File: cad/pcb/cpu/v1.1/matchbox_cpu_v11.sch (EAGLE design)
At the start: 61 parts, among them CN1 SM02B-SRSS-TB, P1 DF12-32-DP, P2 DF12-32-DP, Q1 FDN360P, Q2 FDN360P, U1 STM32F415R, U2 MCP1703, U3 MCP73831, U4 LTC2954-2, Y1 16MHz(9pF)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

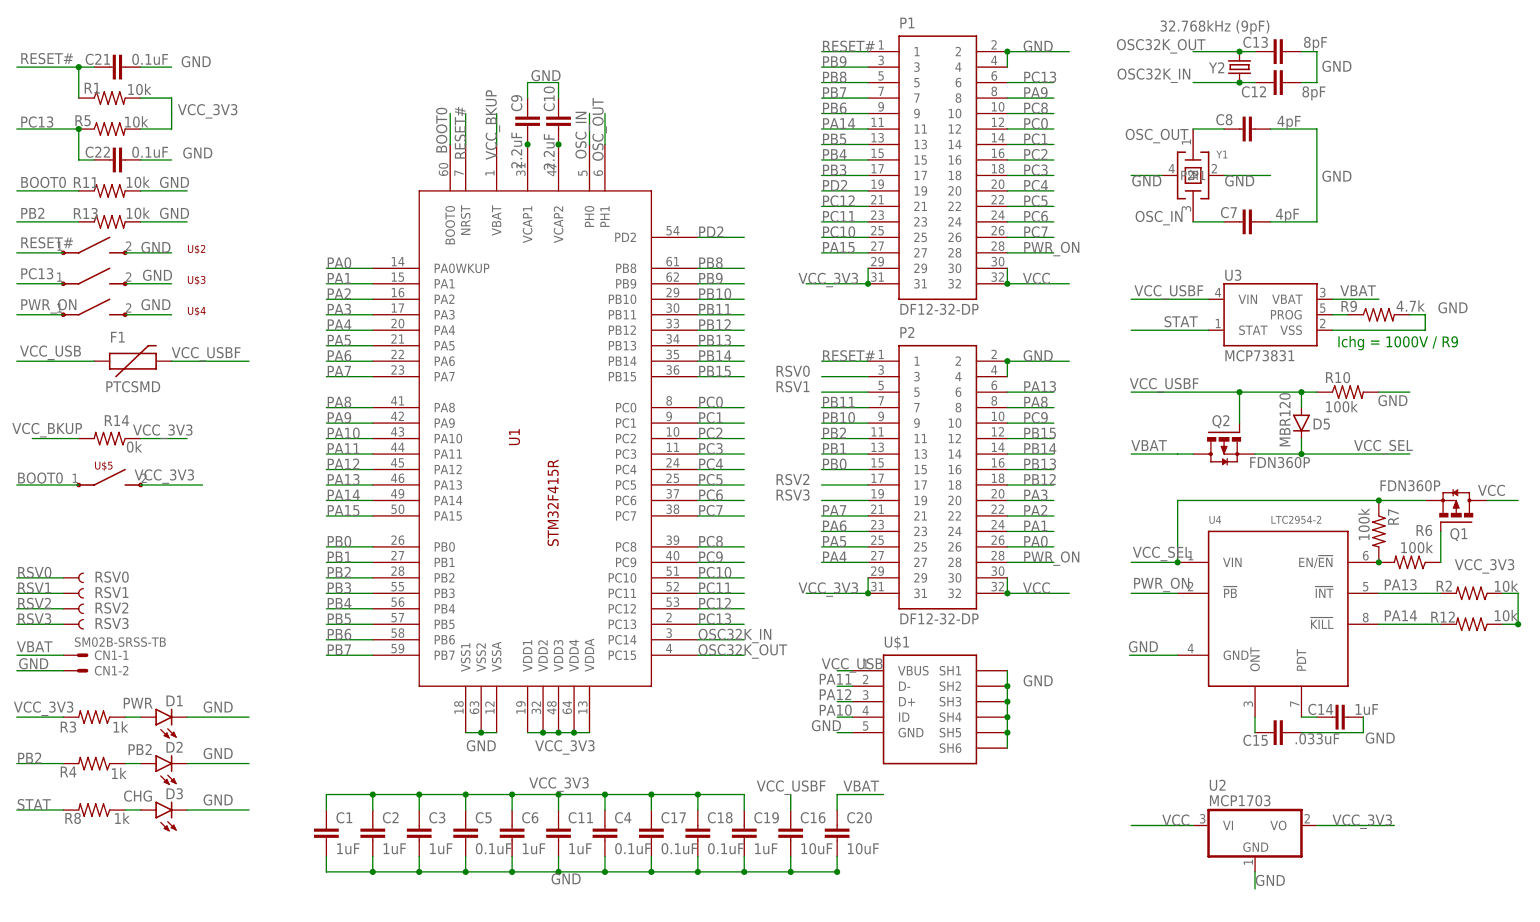
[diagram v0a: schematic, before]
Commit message: Side button improvement
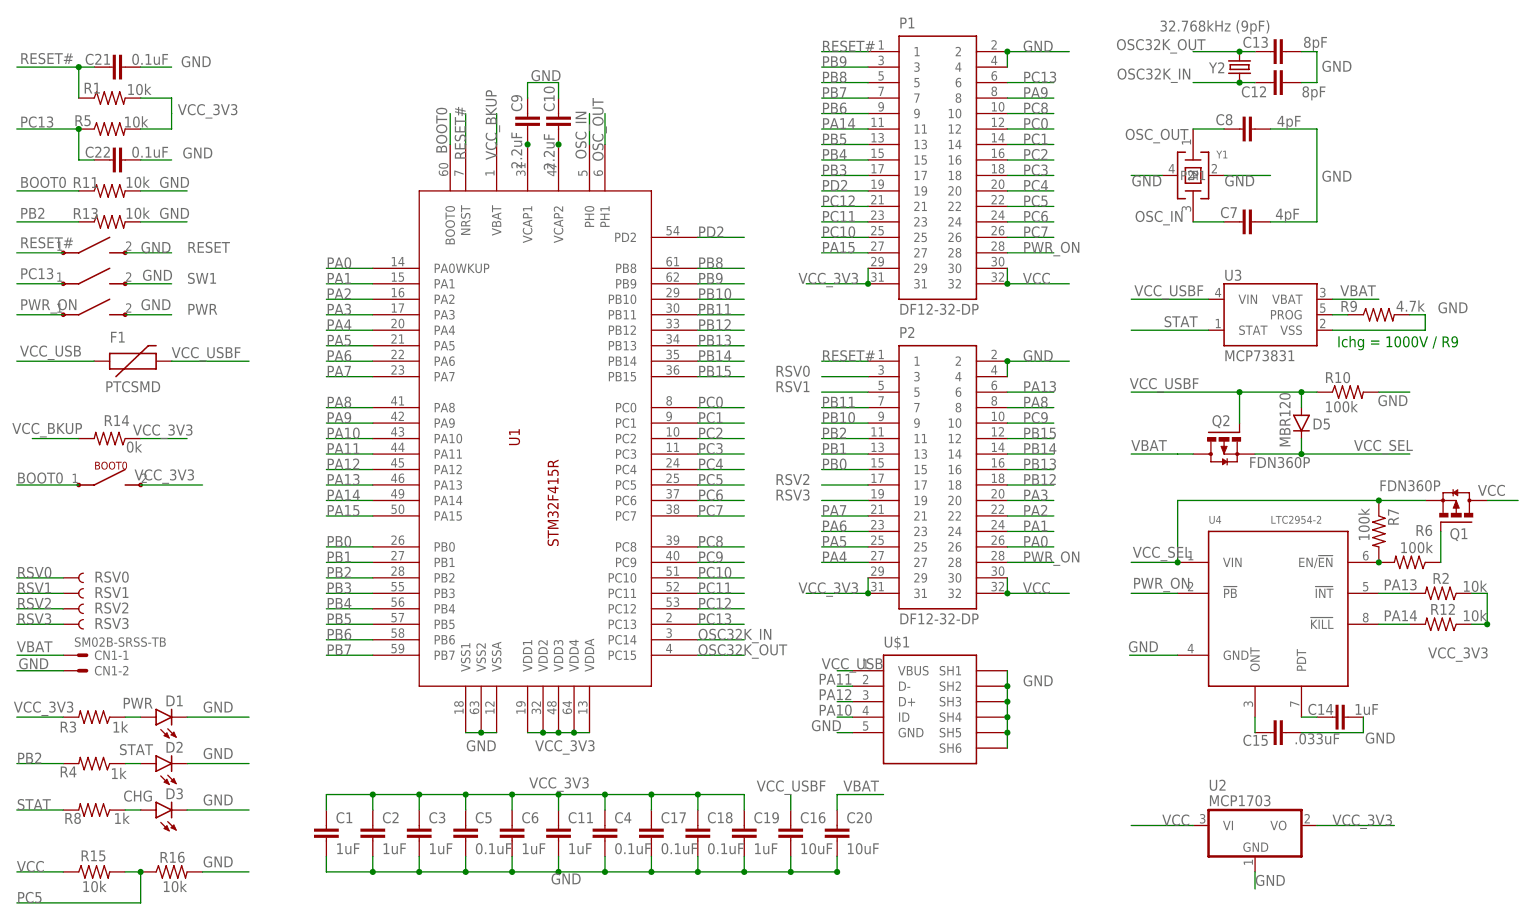
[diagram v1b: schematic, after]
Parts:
- added R15, R16: 10k, SparkFun-Passives:RESISTOR0805-RES
- D2: value PB2 -> STAT
- renumbered U$2 to RESET, U$3 to SW1, U$4 to PWR, U$5 to BOOT0
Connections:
- net GND: now also R16.2
- net PC5: now also R15.2, R16.1
- net VCC: now also R15.1
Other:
- moved on the sheet: R12, R2
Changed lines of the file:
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@@
 <part name="C15" library="SparkFun-Capacitors" deviceset="CAP" device="0805" value=".033uF"/>
 <part name="D1" library="SparkFun-LED" deviceset="LED" device="0603" value="PWR"/>
-<part name="D2" library="SparkFun-LED" deviceset="LED" device="0603" value="PB2"/>
+<part name="D2" library="SparkFun-LED" deviceset="LED" device="0603" value="STAT"/>
 <part name="R3" library="SparkFun-Passives" deviceset="RESISTOR" device="0805-RES" value="1k"/>
 <part name="R4" library="SparkFun-Passives" deviceset="RESISTOR" device="0805-RES" value="1k"/>
@@
 <part name="C22" library="SparkFun-Capacitors" deviceset="CAP" device="0805" value="0.1uF"/>
 <part name="U$1" library="jimduino" deviceset="MICROUSB" device=""/>
-<part name="U$2" library="sharp_display" deviceset="B3U-3100PM-B" device=""/>
-<part name="U$3" library="sharp_display" deviceset="B3U-3100PM-B" device=""/>
-<part name="U$4" library="sharp_display" deviceset="B3U-3100PM-B" device=""/>
-<part name="U$5" library="sharp_display" deviceset="B3U-3100PM-B" device=""/>
+<part name="RESET" library="sharp_display" deviceset="B3U-3100PM-B" device=""/>
+<part name="SW1" library="sharp_display" deviceset="B3U-3100PM-B" device=""/>
+<part name="PWR" library="sharp_display" deviceset="B3U-3100PM-B" device=""/>
+<part name="BOOT0" library="sharp_display" deviceset="B3U-3100PM-B" device=""/>
+<part name="R15" library="SparkFun-Passives" deviceset="RESISTOR" device="0805-RES" value="10k"/>
+<part name="R16" library="SparkFun-Passives" deviceset="RESISTOR" device="0805-RES" value="10k"/>
 </parts>
 <sheets>
@@
 <attribute name="NAME" x="-22.86" y="65.278" size="1.778" layer="95"/>
 </instance>
-<instance part="R2" gate="G$1" x="203.2" y="66.04" smashed="yes" rot="R180">
-<attribute name="NAME" x="200.152" y="68.0974" size="1.778" layer="95" rot="R180"/>
-<attribute name="VALUE" x="210.82" y="68.072" size="1.778" layer="96" rot="R180"/>
+<instance part="R2" gate="G$1" x="198.12" y="66.04" smashed="yes" rot="R180">
+<attribute name="NAME" x="199.644" y="69.3674" size="1.778" layer="95" rot="R180"/>
+<attribute name="VALUE" x="205.74" y="68.072" size="1.778" layer="96" rot="R180"/>
 </instance>
 <instance part="R5" gate="G$1" x="-20.32" y="142.24" smashed="yes">
@@
 <attribute name="VALUE" x="166.624" y="86.614" size="1.778" layer="96"/>
 </instance>
-<instance part="R12" gate="G$1" x="203.2" y="60.96" smashed="yes" rot="R180">
-<attribute name="NAME" x="200.66" y="63.0174" size="1.778" layer="95" rot="R180"/>
-<attribute name="VALUE" x="210.82" y="63.246" size="1.778" layer="96" rot="R180"/>
+<instance part="R12" gate="G$1" x="198.12" y="60.96" smashed="yes" rot="R180">
+<attribute name="NAME" x="200.66" y="64.2874" size="1.778" layer="95" rot="R180"/>
+<attribute name="VALUE" x="205.74" y="63.246" size="1.778" layer="96" rot="R180"/>
 </instance>
 <instance part="D5" gate="G$1" x="175.26" y="93.98" smashed="yes" rot="R270">
@@
 </instance>
 <instance part="U$1" gate="G$1" x="114.3" y="48.26"/>
-<instance part="U$2" gate="G$1" x="-22.86" y="121.92" smashed="yes">
-<attribute name="NAME" x="-7.62" y="121.92" size="1.27" layer="94"/>
-</instance>
-<instance part="U$3" gate="G$1" x="-22.86" y="116.84" smashed="yes">
-<attribute name="NAME" x="-7.62" y="116.84" size="1.27" layer="94"/>
-</instance>
-<instance part="U$4" gate="G$1" x="-22.86" y="111.76" smashed="yes">
-<attribute name="NAME" x="-7.62" y="111.76" size="1.27" layer="94"/>
-</instance>
-<instance part="U$5" gate="G$1" x="-20.32" y="83.82" smashed="yes">
+<instance part="RESET" gate="G$1" x="-22.86" y="121.92" smashed="yes">
+<attribute name="NAME" x="-7.62" y="121.92" size="1.778" layer="95"/>
+</instance>
+<instance part="SW1" gate="G$1" x="-22.86" y="116.84" smashed="yes">
+<attribute name="NAME" x="-7.62" y="116.84" size="1.778" layer="95"/>
+</instance>
+<instance part="PWR" gate="G$1" x="-22.86" y="111.76" smashed="yes">
+<attribute name="NAME" x="-7.62" y="111.76" size="1.778" layer="95"/>
+</instance>
+<instance part="BOOT0" gate="G$1" x="-20.32" y="83.82" smashed="yes">
 <attribute name="NAME" x="-22.86" y="86.36" size="1.27" layer="94"/>
+</instance>
+<instance part="R15" gate="G$1" x="-22.86" y="20.32" smashed="yes">
+<attribute name="NAME" x="-25.146" y="22.0726" size="1.778" layer="95"/>
+<attribute name="VALUE" x="-24.892" y="17.018" size="1.778" layer="96"/>
+</instance>
+<instance part="R16" gate="G$1" x="-10.16" y="20.32" smashed="yes">
+<attribute name="NAME" x="-12.192" y="21.8186" size="1.778" layer="95"/>
+<attribute name="VALUE" x="-11.684" y="17.018" size="1.778" layer="96"/>
 </instance>
 </instances>
@@
 </segment>
 <segment>
-<label x="200.406" y="69.85" size="1.778" layer="95"/>
+<label x="205.994" y="57.15" size="1.778" layer="95" rot="R180"/>
 <pinref part="R12" gate="G$1" pin="1"/>
-<wire x1="208.28" y1="60.96" x2="210.82" y2="60.96" width="0.1524" layer="91"/>
-<junction x="210.82" y="60.96"/>
+<wire x1="203.2" y1="60.96" x2="205.74" y2="60.96" width="0.1524" layer="91"/>
+<junction x="205.74" y="60.96"/>
 <pinref part="R2" gate="G$1" pin="1"/>
-<wire x1="208.28" y1="66.04" x2="210.82" y2="66.04" width="0.1524" layer="91"/>
-<wire x1="210.82" y1="66.04" x2="210.82" y2="60.96" width="0.1524" layer="91"/>
+<wire x1="203.2" y1="66.04" x2="205.74" y2="66.04" width="0.1524" layer="91"/>
+<wire x1="205.74" y1="66.04" x2="205.74" y2="60.96" width="0.1524" layer="91"/>
 </segment>
 <segment>
@@
 <wire x1="-5.08" y1="83.82" x2="-15.24" y2="83.82" width="0.1524" layer="91"/>
 <label x="-16.256" y="84.582" size="1.778" layer="95"/>
-<pinref part="U$5" gate="G$1" pin="P$2"/>
+<pinref part="BOOT0" gate="G$1" pin="P$2"/>
 </segment>
 <segment>
@@
 <wire x1="-17.78" y1="121.92" x2="-10.16" y2="121.92" width="0.1524" layer="91"/>
 <label x="-15.24" y="121.92" size="1.778" layer="95"/>
-<pinref part="U$2" gate="G$1" pin="P$2"/>
+<pinref part="RESET" gate="G$1" pin="P$2"/>
 </segment>
 <segment>
 <wire x1="-10.16" y1="111.76" x2="-17.78" y2="111.76" width="0.1524" layer="91"/>
 <label x="-15.24" y="112.522" size="1.778" layer="95"/>
-<pinref part="U$4" gate="G$1" pin="P$2"/>
+<pinref part="PWR" gate="G$1" pin="P$2"/>
 </segment>
 <segment>
 <wire x1="-10.16" y1="116.84" x2="-17.78" y2="116.84" width="0.1524" layer="91"/>
 <label x="-14.986" y="117.348" size="1.778" layer="95"/>
-<pinref part="U$3" gate="G$1" pin="P$2"/>
+<pinref part="SW1" gate="G$1" pin="P$2"/>
+</segment>
+<segment>
+<wire x1="2.54" y1="20.32" x2="-5.08" y2="20.32" width="0.1524" layer="91"/>
+<label x="0" y="22.86" size="1.778" layer="95" rot="R180"/>
+<pinref part="R16" gate="G$1" pin="2"/>
 </segment>
 </net>
@@
 <pinref part="P1" gate="G$1" pin="22"/>
 </segment>
+<segment>
+<pinref part="R15" gate="G$1" pin="2"/>
+<pinref part="R16" gate="G$1" pin="1"/>
+<wire x1="-15.24" y1="20.32" x2="-17.78" y2="20.32" width="0.1524" layer="91"/>
+<wire x1="-15.24" y1="20.32" x2="-15.24" y2="15.24" width="0.1524" layer="91"/>
+<wire x1="-15.24" y1="15.24" x2="-35.56" y2="15.24" width="0.1524" layer="91"/>
+<junction x="-15.24" y="20.32"/>
+<label x="-35.56" y="15.24" size="1.778" layer="95"/>
+</segment>
 </net>
 <net name="PB0" class="0">
@@
 </segment>
 <segment>
-<wire x1="187.96" y1="60.96" x2="195.58" y2="60.96" width="0.1524" layer="91"/>
+<wire x1="187.96" y1="60.96" x2="193.04" y2="60.96" width="0.1524" layer="91"/>
 <label x="188.722" y="61.468" size="1.778" layer="95"/>
 <pinref part="U4" gate="G$1" pin="!KILL!"/>
 <pinref part="R12" gate="G$1" pin="2"/>
-<wire x1="195.58" y1="60.96" x2="198.12" y2="60.96" width="0.1524" layer="91"/>
 </segment>
 </net>
@@
 <wire x1="-35.56" y1="121.92" x2="-27.94" y2="121.92" width="0.1524" layer="91"/>
 <label x="-35.052" y="122.682" size="1.778" layer="95"/>
-<pinref part="U$2" gate="G$1" pin="P$1"/>
+<pinref part="RESET" gate="G$1" pin="P$1"/>
 </segment>
 </net>
@@
 <wire x1="-27.94" y1="116.84" x2="-35.56" y2="116.84" width="0.1524" layer="91"/>
 <label x="-35.052" y="117.602" size="1.778" layer="95"/>
-<pinref part="U$3" gate="G$1" pin="P$1"/>
+<pinref part="SW1" gate="G$1" pin="P$1"/>
 </segment>
 </net>
@@
 <wire x1="-27.94" y1="111.76" x2="-35.56" y2="111.76" width="0.1524" layer="91"/>
 <label x="-35.052" y="112.522" size="1.778" layer="95"/>
-<pinref part="U$4" gate="G$1" pin="P$1"/>
+<pinref part="PWR" gate="G$1" pin="P$1"/>
 </segment>
 </net>
@@
 </segment>
 <segment>
-<wire x1="187.96" y1="66.04" x2="195.58" y2="66.04" width="0.1524" layer="91"/>
+<wire x1="187.96" y1="66.04" x2="193.04" y2="66.04" width="0.1524" layer="91"/>
 <label x="188.722" y="66.548" size="1.778" layer="95"/>
 <pinref part="U4" gate="G$1" pin="!INT!"/>
 <pinref part="R2" gate="G$1" pin="2"/>
-<wire x1="195.58" y1="66.04" x2="198.12" y2="66.04" width="0.1524" layer="91"/>
 </segment>
 </net>
@@
 <wire x1="-35.56" y1="83.82" x2="-25.4" y2="83.82" width="0.1524" layer="91"/>
 <label x="-35.56" y="84.074" size="1.778" layer="95"/>
-<pinref part="U$5" gate="G$1" pin="P$1"/>
+<pinref part="BOOT0" gate="G$1" pin="P$1"/>
 </segment>
 <segment>
@@
 <label x="152.4" y="27.94" size="1.778" layer="95"/>
 </segment>
-</net>
+<segment>
+<wire x1="-27.94" y1="20.32" x2="-35.56" y2="20.32" width="0.1524" layer="91"/>
+<label x="-35.56" y="20.32" size="1.778" layer="95"/>
+<pinref part="R15" gate="G$1" pin="1"/>
+</segment>
+</net>
